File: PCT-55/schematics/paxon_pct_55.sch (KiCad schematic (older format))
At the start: 618 parts, among them IC1 TA7607AP, IC2 UPC1382C, IC201 HA11431, IC202 TA7676AP, IC301 HA11423, IC502 NEC uPC574, IC901 TC4052BP, IC902 TC4052BP, IC950 HD7407, J1 Audiojack with switch, J401 CONN_01x05, J403 CONN_01x04, J404 CONN_01x07, J503 CONN_01x04, J503-1 CONN_01x04, J505 CONN_01x02, J903 CONN_01x02, J913 CONN_01x05, J915 CONN_01x11, J918 CONN_01x02, J919 CONN_01x04, J920 CONN_01x08, J921 CONN_01x06, J924 Centronics 14-pin, J927 CONN_01x03, K1 CONN_01x03, P402 CONN_01x03, P504 CONN_01x09, P801 CONN_01x03, P802 CONN_01x03, P901 CONN_01x09, P902 CONN_01x06, P903 CONN_01x02, P911 CONN_01x05, P912 CONN_01x02, P913 CONN_01x05, P914 CONN_01x04, P917 CONN_01x02, P918 CONN_01x02, P919 CONN_01x04, P927 CONN_01x03, Q1 C388A_NPN_BCE, Q2 C2458_NPN_BCE, Q202 A854_PNP_BCE, Q203 A1015_PNP_BCE, Q204 A1015_PNP_BCE, Q301 C2073_NPN_BCE, Q302 C2073_NPN_BCE, Q303 A1015_PNP_BCE, Q304 C1815_NPN_BCE, Q351 C2610_NPN_BCE, Q352 D1425_NPN_BCE, Q451 D758_NPN_BCE, Q452 D758_NPN_BCE, Q453 D758_NPN_BCE, Q454 C1815_NPN_BCE, Q455 C1815_NPN_BCE, Q456 C1815_NPN_BCE, Q501 A1015_PNP_BCE, Q502 C1815_NPN_BCE, Q503 C2236_NPN_CBE, Q504 2SC2122A_NPN_BCE, Q505 D1052A_NPN_BCE, Q551 A733_PNP_BCE, Q801 C1815_NPN_BCE, Q802 A950_PNP_BCE, Q803 C2120_NPN_BCE, Q901 A952_PNP_BCE, Q902 C1815_NPN_BCE, Q903 A733_PNP_BCE, Q905 ???, Q906 ???, Q950 C1815_NPN_BCE, Q951 A950_PNP_BCE, Q952 C2120_NPN_BCE, Q953 C1815_NPN_BCE, Q954 C1815_NPN_BCE, Q955 C1815_NPN_BCE, SW1 CH1, SW10 MSX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

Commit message: added all variable resistors marked values
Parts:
- added B: ., symbol agg-kicad:CONN_01x03
- added D: CONN_01x02, symbol agg-kicad:CONN_01x02
- added J802: CONN_01x03, symbol agg-kicad:CONN_01x03
- added R304: 2K2, symbol agg-kicad:R
- added VR301: 5KB - 421a, symbol Device:R_POT
- added VR802: 850K, symbol Device:R_POT
- F501: value FUSE -> 4A?
- VR1: value ??? -> 52
- VR206: renamed from VR208; value ??? -> 1KB - 463a
- VR207, VR252: value ??? -> 10KB-431a
- VR251, VR254: value ??? -> 14
- VR302: value 266R -> 501 - 1
- VR351: value 4K9 -> 103
- VR352: value 1K544 -> 23
- VR451: value 220R -> 23 -
- VR452: value 220R -> 23 - ?
- VR453: renamed from VR353; value 220R -> 23 - ?
- VR454: value 1K7 -> 23 - 1K7?
- VR455: value 1K7 -> 23 - 1K7
- VR501: value 820R -> 13 - 820R ???
- VR950: value 340R -> 52 - 340R?
- VR951: value 370R -> 52 - 370R?
- VR952: value 8K8 -> 54
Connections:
- net labels added: BBB_brown_wire, BBB_gray_wire
- wire segments 2488 -> 2507
- no-connect marks 8 -> 9
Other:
- note added: "(AAA) wires to A connector\nin Power switch PCB (volume)\n"
- note added: "(AAA) wires to P802\nin main PCB"
- note added: "(BBB) wires"
- note added: "Variable coil"
- note added: "to DEGAUS\nwires"
- note removed: "VR???\nValue???"
- note removed: "to Volume pot\n(AAA) wires"
- moved on the sheet: R501, TH501

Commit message: some VRxxx ohm values added
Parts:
- VR1: value 52 -> 52 - 2K07
- VR352: value 23 -> 23 - 1K544
- VR952: value 54 -> 54 - 8K8
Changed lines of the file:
@@
 P 4490 960
 F 0 "VR952" H 4420 990 50  0000 R CNN
-F 1 "54" H 4420 915 50  0000 R CNN
+F 1 "54 - 8K8" H 4420 915 50  0000 R CNN
 F 2 "" H 4490 960 50  0001 C CNN
 F 3 "~" H 4490 960 50  0001 C CNN
@@
 P 4040 940
 F 0 "C955" H 3750 950 50  0000 L CNN
-F 1 "1uf/50v" H 3870 800 50  0000 L CNN
+F 1 "1uf/50v" H 3670 870 50  0000 L CNN
 F 2 "" H 4040 940 50  0001 C CNN
 F 3 "~" H 4040 940 50  0001 C CNN
@@
 P 9660 13490
 F 0 "VR352" H 9580 13460 50  0000 R CNN
-F 1 "23" H 9560 13560 50  0000 R CNN
+F 1 "23 - 1K544" H 9560 13560 50  0000 R CNN
 F 2 "" H 9660 13490 50  0001 C CNN
 F 3 "~" H 9660 13490 50  0001 C CNN
@@
 P 26260 2820
 F 0 "VR1" H 26190 2850 50  0000 R CNN
-F 1 "52" H 26160 2770 50  0000 R CNN
+F 1 "52 - 2K07" H 26200 2770 50  0000 R CNN
 F 2 "" H 26260 2820 50  0001 C CNN
 F 3 "~" H 26260 2820 50  0001 C CNN

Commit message: VR value added
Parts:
- VR251, VR254: value 14 -> 14 - 7K6
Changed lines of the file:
@@
 P 18330 13190
 F 0 "VR254" H 18260 13220 50  0000 R CNN
-F 1 "14" H 18230 13140 50  0000 R CNN
+F 1 "14 - 7K6" H 18230 13140 50  0000 R CNN
 F 2 "" H 18330 13190 50  0001 C CNN
 F 3 "~" H 18330 13190 50  0001 C CNN
@@
 P 18320 14150
 F 0 "VR251" H 18250 14180 50  0000 R CNN
-F 1 "14" H 18220 14100 50  0000 R CNN
+F 1 "14 - 7K6" H 18220 14100 50  0000 R CNN
 F 2 "" H 18320 14150 50  0001 C CNN
 F 3 "~" H 18320 14150 50  0001 C CNN

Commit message: Add files via upload
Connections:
- wire segments 2507 -> 2506
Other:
- moved on the sheet: C308, C309, D302, D303, R309, R310, R312, R315

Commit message: Add files via upload
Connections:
- wire segments 2506 -> 2498
- no-connect marks 9 -> 10
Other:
- note added: "When measuring resistance between transformer pins:\n-1,2,4,5,8,9 have about zero ohms between themselfs\n-3,6,10 have about zero ohms between themselfs"
- note added: "pin 6 is not connected"
- note removed: "When measuring resistance between transformer pins:\n-1,2,4,5,8,9 have about zero ohms between themselfs\n-3,5,10 have about zero ohms between themselfs"
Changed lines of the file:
@@
 Text GLabel 12620 13630 2    50   Input ~ 0
 IC202_FieldBlanking
-Text GLabel 9890 14720 2    50   Input ~ 0
+Text GLabel 9980 14680 2    50   Input ~ 0
 FLYBACK_pin_3
 $Comp
@@
 Wire Wire Line
 	9130 14290 9130 14540
-Wire Wire Line
-	9130 14290 9130 14170
 Connection ~ 9130 14290
 Wire Wire Line
@@
 $EndComp
 Wire Wire Line
-	9230 14170 9230 14180
-Connection ~ 9130 14170
-Wire Wire Line
-	9130 14170 9130 14030
-Wire Wire Line
-	9130 14170 9230 14170
-Connection ~ 9230 14170
-Wire Wire Line
-	9230 14170 9470 14170
-Wire Wire Line
 	8750 14290 8750 14130
 Wire Wire Line
@@
 	9470 13490 9510 13490
 Wire Wire Line
-	9470 13490 9470 14170
-Wire Wire Line
 	9660 13630 9660 13640
 Wire Wire Line
@@
 $EndComp
 Wire Wire Line
-	9890 14540 9890 14870
+	9890 14540 9890 14680
 Wire Wire Line
 	9890 14970 9890 15000
@@
 Wire Wire Line
 	7840 15280 8100 15280
-Wire Wire Line
-	9140 14030 9130 14030
-Wire Wire Line
-	7930 14030 7930 14050
-Wire Wire Line
-	7930 14050 7050 14050
-Connection ~ 9130 14030
-Wire Wire Line
-	9130 14030 7930 14030
-Connection ~ 7050 14050
-Wire Wire Line
-	7050 14050 7040 14050
 Text GLabel 3870 13160 2    50   Input ~ 0
 J920_pin_2
@@
 $EndComp
 Wire Wire Line
-	6060 14600 6050 14600
-Connection ~ 6050 14600
-Wire Wire Line
 	4070 14420 4070 14460
 Wire Wire Line
@@
 Connection ~ 4800 14460
 Wire Wire Line
-	6060 14050 6050 14050
-Connection ~ 6050 14050
-Wire Wire Line
 	2310 14240 2310 14820
 Wire Wire Line
@@
 	5680 14460 5680 14780
 Wire Wire Line
-	7060 14600 7230 14600
-Wire Wire Line
 	7230 14600 7230 15880
 Wire Wire Line
@@
 	8920 10930 9160 10930
 Wire Wire Line
-	9360 10930 9410 10930
-Wire Wire Line
 	9880 12500 9730 12500
 Wire Wire Line
@@
 	10170 10940 11370 10940
 Wire Wire Line
-	10530 12020 10530 11250
-Wire Wire Line
 	8730 15860 8730 15950
 Wire Wire Line
@@
 P301
 Connection ~ 9410 10380
-Connection ~ 9410 10930
 Wire Wire Line
 	9410 10380 9670 10380
 Wire Wire Line
-	9410 10930 9860 10930
-Wire Wire Line
 	9670 10450 9670 10380
 Connection ~ 9670 10380
 Wire Wire Line
 	9670 10380 9850 10380
-Wire Wire Line
-	9410 10650 9410 10930
 Text GLabel 9170 6370 0    50   Input ~ 0
 15V_
@@
 FLYBACK transformer\nfrom solder side
 Text Notes 3210 9970 0    50   ~ 0
-When measuring resistance between transformer pins:\n-1,2,4,5,8,9 have about zero ohms between themselfs\n-3,5,10 have about zero ohms between themselfs
+When measuring resistance between transformer pins:\n-1,2,4,5,8,9 have about zero ohms between themselfs\n-3,6,10 have about zero ohms between themselfs
 Text Notes 18850 3970 0    50   ~ 0
 G\nR\nB
@@
 	5090 14820 2310 14820
 Wire Wire Line
-	5090 14050 6050 14050
-Wire Wire Line
 	5170 14600 5170 14460
 Wire Wire Line
-	5170 14600 6050 14600
-Wire Wire Line
 	5420 14460 5260 14460
 Wire Wire Line
@@
 Wire Notes Line
 	7620 12320 8070 12320
+NoConn ~ 2070 10880
+Text Notes 460  10970 0    51   ~ 0
+pin 6 is not connected
+Wire Wire Line
+	9360 10930 9410 10930
+Wire Wire Line
+	9410 10660 9410 10930
+Connection ~ 9410 10930
+Wire Wire Line
+	9410 10930 9860 10930
+Wire Wire Line
+	9890 14680 9980 14680
+Connection ~ 9890 14680
+Wire Wire Line
+	9890 14680 9890 14870
+Wire Wire Line
+	9130 14290 9470 14290
+Wire Wire Line
+	9130 14050 9130 14290
+Wire Wire Line
+	9470 13490 9470 14290
+Wire Wire Line
+	7050 14050 9130 14050
+Wire Wire Line
+	7050 14600 7230 14600
+Wire Wire Line
+	6050 14600 5170 14600
+Wire Wire Line
+	6050 14050 5090 14050
 $EndSCHEMATC

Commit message: corrected 4CEE pin mappings to P301 pins and gnd
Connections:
- wire segments 2498 -> 2500
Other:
- moved on the sheet: C365, C389, L388, L389, R4000
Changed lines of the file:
@@
 $EndComp
 Wire Wire Line
-	11250 10750 11250 11590
-Wire Wire Line
 	13520 14570 13520 14840
 Wire Wire Line
@@
 L agg-kicad:L L389
 U 1 1 88DF0688
-P 11040 11250
-F 0 "L389" H 11120 11320 50  0000 C CNN
-F 1 "4.7mH" H 11100 11200 50  0000 C CNN
-F 2 "" H 11040 11250 50  0001 C CNN
-F 3 "" H 11040 11250 50  0001 C CNN
-	1    11040 11250
+P 11080 11250
+F 0 "L389" H 11160 11320 50  0000 C CNN
+F 1 "4.7mH" H 11140 11200 50  0000 C CNN
+F 2 "" H 11080 11250 50  0001 C CNN
+F 3 "" H 11080 11250 50  0001 C CNN
+	1    11080 11250
 	1    0    0    -1
 $EndComp
@@
 L agg-kicad:R R389
 U 1 1 88DF2FE0
-P 11370 11250
-F 0 "R389" H 11400 11310 50  0000 C CNN
-F 1 "220R" H 11430 11190 50  0000 C CNN
-F 2 "" H 11370 11250 50  0001 C CNN
-F 3 "" H 11370 11250 50  0001 C CNN
-	1    11370 11250
+P 11360 11250
+F 0 "R389" H 11390 11310 50  0000 C CNN
+F 1 "220R" H 11420 11190 50  0000 C CNN
+F 2 "" H 11360 11250 50  0001 C CNN
+F 3 "" H 11360 11250 50  0001 C CNN
+	1    11360 11250
 	1    0    0    -1
 $EndComp
-Wire Wire Line
-	11370 11250 11140 11250
 $Comp
 L agg-kicad:C C389
 U 1 1 88F5CAC1
-P 11610 11250
-F 0 "C389" H 11660 11320 50  0000 C CNN
-F 1 "330nF" H 11660 11170 50  0000 C CNN
-F 2 "" H 11610 11250 50  0001 C CNN
-F 3 "" H 11610 11250 50  0001 C CNN
-	1    11610 11250
-	1    0    0    -1
+P 11720 11080
+F 0 "C389" V 11750 10940 50  0000 C CNN
+F 1 "330nF" V 11680 10930 50  0000 C CNN
+F 2 "" H 11720 11080 50  0001 C CNN
+F 3 "" H 11720 11080 50  0001 C CNN
+	1    11720 11080
+	0    -1   -1   0
 $EndComp
 $Comp
 L agg-kicad:C C365
 U 1 1 890C47AC
-P 11840 11510
-F 0 "C365" V 11930 11660 50  0000 C CNN
-F 1 "330nF" V 11820 11660 50  0000 C CNN
-F 2 "" H 11840 11510 50  0001 C CNN
-F 3 "" H 11840 11510 50  0001 C CNN
-	1    11840 11510
+P 11720 11510
+F 0 "C365" V 11820 11400 50  0000 C CNN
+F 1 "330nF" V 11710 11380 50  0000 C CNN
+F 2 "" H 11720 11510 50  0001 C CNN
+F 3 "" H 11720 11510 50  0001 C CNN
+	1    11720 11510
 	0    -1   -1   0
 $EndComp
@@
 U 1 1 8922D6AF
 P 12160 11880
-F 0 "C378" V 12210 12060 50  0000 C CNN
-F 1 "56nF/200v" V 12290 11880 50  0000 C CNN
+F 0 "C378" V 12300 11760 50  0000 C CNN
+F 1 "56nF/200v" V 12210 11610 50  0000 C CNN
 F 2 "" H 12160 11880 50  0001 C CNN
 F 3 "" H 12160 11880 50  0001 C CNN
@@
 $EndComp
 Wire Wire Line
-	11710 11250 11840 11250
-Wire Wire Line
-	11840 11510 11840 11590
-Wire Wire Line
-	11840 11590 11250 11590
-Connection ~ 11250 11590
-Wire Wire Line
-	11610 11250 11470 11250
-Wire Wire Line
-	11840 11250 11840 10950
-Wire Wire Line
-	11840 10950 11730 10950
-Connection ~ 11840 11250
+	11720 11510 11720 11590
 $Comp
 L agg-kicad:L L388
 U 1 1 89C21EDD
-P 11460 10810
-F 0 "L388" H 11510 10870 50  0000 C CNN
-F 1 "00257" H 11810 10870 50  0000 C CNN
-F 2 "" H 11460 10810 50  0001 C CNN
-F 3 "" H 11460 10810 50  0001 C CNN
-	1    11460 10810
+P 11290 10820
+F 0 "L388" H 11340 10880 50  0000 C CNN
+F 1 "00257" H 11640 10880 50  0000 C CNN
+F 2 "" H 11290 10820 50  0001 C CNN
+F 3 "" H 11290 10820 50  0001 C CNN
+	1    11290 10820
 	1    0    0    -1
 $EndComp
@@
 L agg-kicad:R R4000
 U 1 1 89D8FC81
-P 11470 11030
-F 0 "R4000" H 11500 11090 50  0000 C CNN
-F 1 "100R" H 11530 10970 50  0000 C CNN
-F 2 "" H 11470 11030 50  0001 C CNN
-F 3 "" H 11470 11030 50  0001 C CNN
-	1    11470 11030
+P 11300 11040
+F 0 "R4000" H 11330 11100 50  0000 C CNN
+F 1 "100R" H 11360 10980 50  0000 C CNN
+F 2 "" H 11300 11040 50  0001 C CNN
+F 3 "" H 11300 11040 50  0001 C CNN
+	1    11300 11040
 	1    0    0    -1
 $EndComp
 Wire Wire Line
-	11570 11030 11730 11030
-Wire Wire Line
-	11730 11030 11730 10950
+	11400 11040 11560 11040
 Wire Wire Line
-	11730 10950 11730 10810
+	11560 10820 11390 10820
 Wire Wire Line
-	11730 10810 11560 10810
-Connection ~ 11730 10950
+	11290 10820 11200 10820
 Wire Wire Line
-	11460 10810 11370 10810
-Wire Wire Line
-	11370 10810 11370 10940
-Wire Wire Line
-	11370 11030 11470 11030
-Connection ~ 11370 10940
-Wire Wire Line
-	11370 10940 11370 11030
+	11200 11040 11300 11040
 Text GLabel 13940 13120 0    50   Input ~ 0
 GREEN_wire_I
@@
 Wire Wire Line
 	11710 14260 11710 14680
-Text GLabel 11840 11170 2    59   Input ~ 0
+Text GLabel 11720 10920 2    59   Input ~ 0
 ThinBlackWire
 Text GLabel 12110 11540 2    59   Input ~ 0
 ThinBlackWire
 Wire Wire Line
-	11840 11250 11840 11410
-Wire Wire Line
 	8920 11460 8920 10930
 Wire Wire Line
@@
 	9890 11880 9800 11880
 Wire Wire Line
-	10170 10940 11370 10940
-Wire Wire Line
 	8730 15860 8730 15950
 Wire Wire Line
@@
 	10350 11300 10590 11300
 Wire Wire Line
-	10590 11300 10590 10750
-Wire Wire Line
 	10590 10750 11250 10750
 Wire Wire Line
@@
 	10750 11890 10850 11890
 Wire Wire Line
-	10750 11590 11250 11590
-Wire Wire Line
 	10670 11250 10670 12250
 Wire Wire Line
 	10670 12250 10860 12250
 Wire Wire Line
-	10670 11250 11040 11250
-Wire Wire Line
 	12110 11610 12160 11610
 Wire Wire Line
@@
 Wire Wire Line
 	6050 14050 5090 14050
+Wire Wire Line
+	10590 10930 10590 11300
+Wire Wire Line
+	11250 10750 11250 10650
+Wire Wire Line
+	11250 10650 11960 10650
+Wire Wire Line
+	11960 10650 11960 11590
+$Comp
+L power:GND #PWR?
+U 1 1 6AE9BB23
+P 10590 10750
+F 0 "#PWR?" H 10590 10500 50  0001 C CNN
+F 1 "GND" H 10600 10800 50  0000 C CNN
+F 2 "" H 10590 10750 50  0001 C CNN
+F 3 "" H 10590 10750 50  0001 C CNN
+	1    10590 10750
+	1    0    0    -1
+$EndComp
+Wire Wire Line
+	11200 10820 11200 10930
+Wire Wire Line
+	10590 10930 11200 10930
+Connection ~ 11200 10930
+Wire Wire Line
+	11200 10930 11200 11040
+Wire Wire Line
+	11560 10820 11560 10920
+Wire Wire Line
+	11720 10980 11720 10920
+Wire Wire Line
+	11720 10920 11560 10920
+Connection ~ 11560 10920
+Wire Wire Line
+	11560 10920 11560 11040
+Wire Wire Line
+	11720 11080 11720 11250
+Wire Wire Line
+	11720 11410 11720 11250
+Wire Wire Line
+	10670 11250 11080 11250
+Wire Wire Line
+	11180 11250 11360 11250
+Wire Wire Line
+	11460 11250 11720 11250
+Wire Wire Line
+	10750 11590 11720 11590
+Connection ~ 11720 11250
+Connection ~ 11720 11590
+Wire Wire Line
+	11720 11590 11960 11590
 $EndSCHEMATC

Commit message: Add files via upload
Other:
- note added: "CEA PCB (AV input + Printer Port)\n-rca video + audio input\n-RGB digital input\n-MSX printer port"
- note added: "DMB PCB (Front panel)\n-channel switches+tuner pots+msx reset/load/run buttons"
- note added: "DNF PCB (Tube neck)"
- note added: "MSX PCB"
- note added: "to generate 32V <---"
- note removed: "AV input + Printer Port PCB:\n-rca video + audio input\n-RGB digital input\n-MSX printer port"
- note removed: "Front panel PCB:\n(channel switches+tuner pots+msx reset/load/run buttons)"
- note removed: "Tube neck PCB"
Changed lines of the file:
@@
 	-340 4780 -340 170
 Text Notes 130  380  0    157  ~ 31
-AV input + Printer Port PCB:\n-rca video + audio input\n-RGB digital input\n-MSX printer port
+CEA PCB (AV input + Printer Port)\n-rca video + audio input\n-RGB digital input\n-MSX printer port
 $Comp
 L agg-kicad:CONN_01x06 P902
@@
 (UUU) wires to CON-6\nin MSX PCB
 Text Notes 9720 520  0    157  ~ 31
-Front panel PCB:\n(channel switches+tuner pots+msx reset/load/run buttons)
+DMB PCB (Front panel)\n-channel switches+tuner pots+msx reset/load/run buttons
 Text Notes 3910 650  0    50   ~ 0
 (OOO) wires to P919\nin 4CEC PCB
@@
 	18080 530  18090 530
 Text Notes 18140 830  0    157  ~ 31
-Tube neck PCB
+DNF PCB (Tube neck)
 Text GLabel 20980 1450 2    50   Input ~ 0
 TUBE_pin_1_2?
@@
 Wire Wire Line
 	19100 2820 19190 2820
-Text Notes 20890 1170 0    50   ~ 0
+Text Notes 20920 1360 0    50   ~ 0
 Separate black thick ground wires towards:\n-tube ground\n-tuner box metal\n-AV input+PrinterPort PCB\n\nThere is also thick black wire from \ndigital RGB pcb to tuner box metal
-Text Notes 20340 730  0    118  ~ 24
+Text Notes 21040 780  0    118  ~ 24
 NOTE!
 Text Notes 3430 10960 0    50   ~ 0
@@
 	3310 3570 3490 3570
 $Sheet
-S 24750 7580 3540 2220
+S 24750 7580 2900 2150
 U 65EF74FD
-F0 "MSX PCB" 51
+F0 "MSX PCB" 118
 F1 "msx_pcb.sch" 51
 $EndSheet
@@
 Wire Wire Line
 	11720 11590 11960 11590
+Text Notes 5980 12230 0    51   ~ 0
+to generate 32V <---
+Text Notes 24760 7390 0    118  ~ 24
+MSX PCB
 $EndSCHEMATC

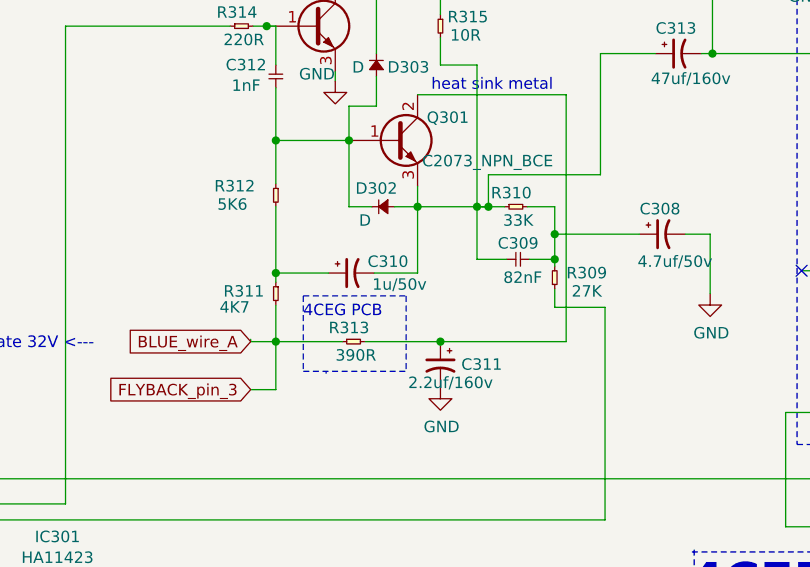
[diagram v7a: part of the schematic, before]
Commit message: corrected vertical drive circuit C310 value
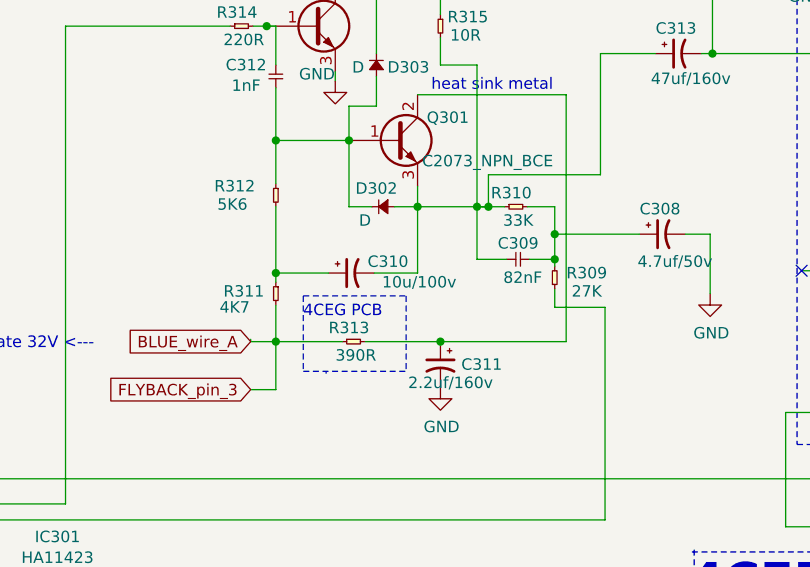
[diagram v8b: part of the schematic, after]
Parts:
- C310: value 1u/50v -> 10u/100v
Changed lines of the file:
@@
 P 7830 11890
 F 0 "C310" V 7780 11640 50  0000 L CNN
-F 1 "1u/50v" V 7880 11560 50  0000 L CNN
+F 1 "10u/100v" V 7870 11430 50  0000 L CNN
 F 2 "" H 7830 11890 50  0001 C CNN
 F 3 "~" H 7830 11890 50  0001 C CNN
